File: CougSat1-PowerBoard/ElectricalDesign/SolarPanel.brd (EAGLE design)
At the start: 79 x 90 mm, 120 parts, among them J101 Wire Harness Connector, U1 INA199C2, U100 SPV1040, U101 SPV1040, U2 INA199C2, U3 INA199C2, U4 INA199C2, U5 AD7291, U6 AD7291, U7 AD8515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

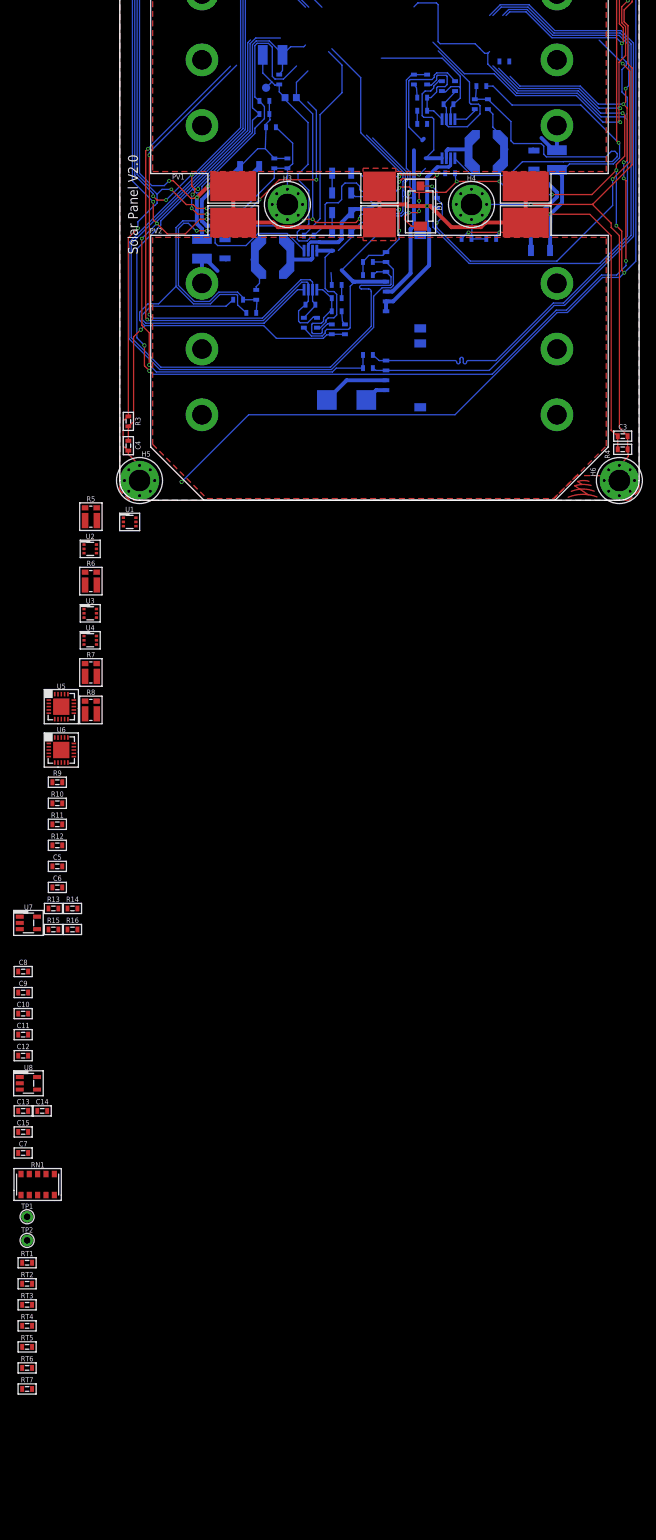
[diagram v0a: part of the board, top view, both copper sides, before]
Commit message: Stuffed addresses on variants, exported PDFs
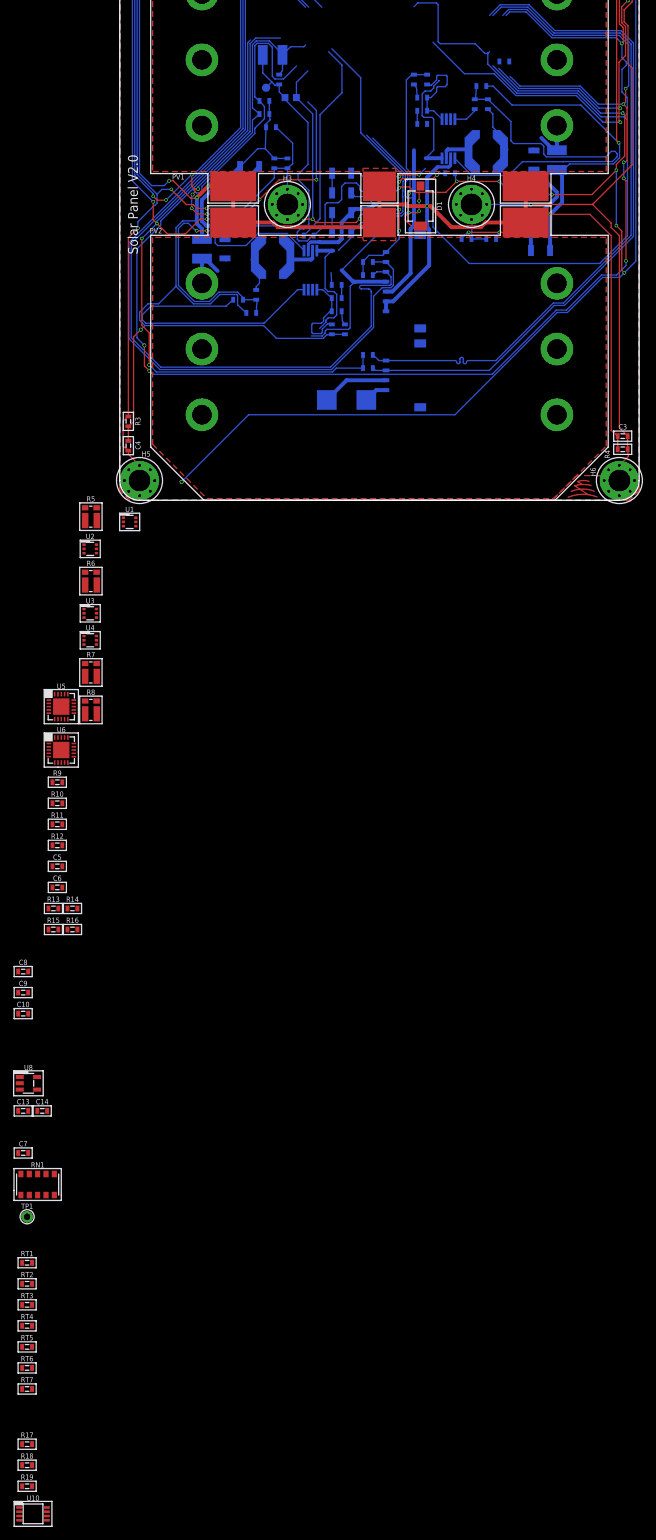
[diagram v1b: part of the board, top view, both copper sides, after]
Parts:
- removed C102, C115, C12: 1µF 10%, CougsInSpace-Capacitors:1608
- removed C11: 10µF 10%, CougsInSpace-Capacitors:1608
- removed C15: 100nF 10%, CougsInSpace-Capacitors:1608
- removed R103, R104, R127, R128: 1kΩ 0.1%, CougsInSpace-Resistors:1608
- removed R115: 150Ω 1%, CougsInSpace-Resistors:1608
- removed TP2: TEST_POINT-THT-1.0, CougsInSpace-Connectors:THT-1.0
- removed U7: AD8515, CougsInSpace-IC-Amplifiers:SOT23-5
- added R17: 10Ω 5%, CougsInSpace-Resistors:1608
- added R18: 33kΩ 1%, CougsInSpace-Resistors:1608
- added R19: 1kΩ 0.1%, CougsInSpace-Resistors:1608
- added U10: AD8542, CougsInSpace-IC-Amplifiers:MSOP-8
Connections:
- net AVREF-1 renamed AVREF
- net N$1 renamed PV_I_N-B
- net N$3 renamed VOUT_N-B
- net N$4 renamed VOUT_P-B
- net N$5 renamed PV_I_N-A
- net N$6 renamed PV_I_P-A
- net N$7 renamed VOUT_N-A
- net N$8 renamed VOUT_P-A
- removed net AVREF-0: C12.1, TP2.1, U7.1, U7.4
- removed net MPPT_ICTRL_N-A: C102.2, R104.1, U100.6
- removed net MPPT_ICTRL_N-B: C115.2, R127.1, U101.6
- removed net MPPT_ICTRL_P-A: C102.1, R103.1, U100.7
- removed net MPPT_ICTRL_P-B: C115.1, R128.1, U101.7
- removed net N$13: C11.1, U5.7, U7.3
- removed net N$16: R5.2-KELVIN
- new net N$1: U101.6, U101.7
- new net PD_AMP_FB: R18.1, R19.2, U10.6
- new net PD_IN: D1.C, R17.1, U10.2
- new net PD_TRANS_OUT: R17.2, U10.1, U10.5
- new net PV_I_P-B: R5.2-KELVIN, U1.4
- net AGND: now also D1.A, R19.1, U10.3, U10.4; no longer C11.2, C12.2, C15.2, R115.1, U7.2
- net AVDD: now also U10.8; no longer C15.1, D1.C, U7.5
- net MPPT_VOUT-A: no longer R103.2
- net MPPT_VOUT-B: no longer R128.2
- net N$2: now also U100.6, U100.7; no longer U1.4
- net PHOTODIODE: now also R18.2, U10.7; no longer D1.A, R115.2
- net VOUT-A: no longer R104.2
- net VOUT-B: no longer R127.2
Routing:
- net MPPT_ICTRL_P-A: track 80.7 -> 0.00 mm, vias 2 -> 0
- net MPPT_ICTRL_N-A: track 77.5 -> 0.00 mm, vias 2 -> 0
- net PHOTODIODE: track 69.6 -> 0.00 mm, vias 4 -> 0
- net MPPT_ICTRL_N-B: track 24.9 -> 0.00 mm
- net MPPT_ICTRL_P-B: track 23.5 -> 0.00 mm
- net VOUT-B: track 55.4 -> 36.9 mm
- net VOUT-A: track 53.4 -> 51.7 mm
- net AVDD: track 292.4 -> 291.0 mm
- net AGND: track 388.7 -> 387.8 mm

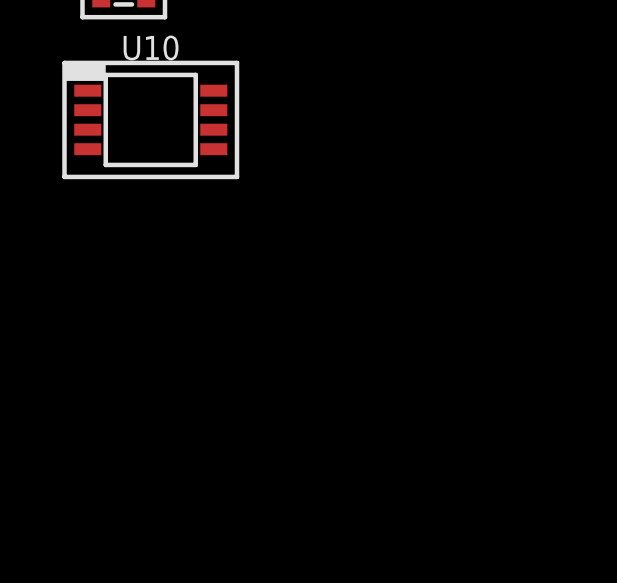
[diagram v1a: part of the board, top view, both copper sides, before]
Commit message: Fixed chematic off-sheet connectors
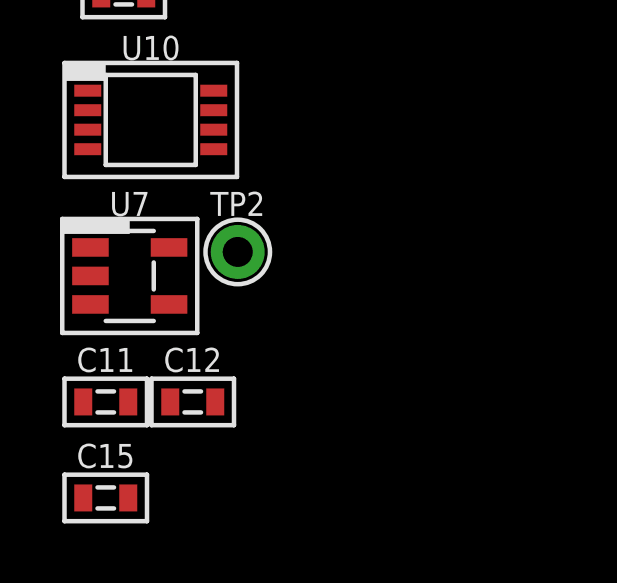
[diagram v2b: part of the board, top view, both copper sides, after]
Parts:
- added C11: 10µF 10%, CougsInSpace-Capacitors:1608
- added C12: 1µF 10%, CougsInSpace-Capacitors:1608
- added C15: 100nF 10%, CougsInSpace-Capacitors:1608
- added TP2: TEST_POINT-THT-1.0, CougsInSpace-Connectors:THT-1.0
- added U7: AD8515, CougsInSpace-IC-Amplifiers:SOT23-5
- J100: value (none) -> ADCS
- J101: value Wire Harness Connector -> EPS
- R100, R101, R110, R112: value 0Ω <20mΩ -> 2.2kΩ 1%
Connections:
- net AVREF renamed AVREF-1
- net N$10 renamed ADC_AS1-EPS
- net N$11 renamed ADC_DCAP-ADCS
- net N$12 renamed ADC_DCAP-EPS
- net N$14 renamed ADC_AS0-ADCS
- net N$15 renamed ADC_AS1-ADCS
- net N$17 renamed ADC_VREF-ADCS
- net N$9 renamed ADC_AS0-EPS
- new net ADC_VREF-EPS: C11.1, U5.7, U7.3
- new net AVREF-0: C12.1, TP2.1, U7.1, U7.4
- net AGND: now also C11.2, C12.2, C15.2, U7.2
- net AVDD: now also C15.1, U7.5
- net VOUT-A: no longer U5.5
- net VOUT-B: no longer U5.4

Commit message: Addressed most feedback points
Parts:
- removed RT100, RT102: 68kΩ 5%, CougsInSpace-Resistors:1608
- added R20, R21: 1kΩ 0.1%, CougsInSpace-Resistors:1608
- added R22, R23: 10kΩ 0.1%, CougsInSpace-Resistors:1608
- added RN2, RN3: 50kΩ 0.1%, CougsInSpace-Resistors:1616
- added RT8, RT9: 10kΩ 5%, CougsInSpace-Resistors:1608
- added TP3, TP4: TEST_POINT-THT-1.0, CougsInSpace-Connectors:THT-1.0
- moved R121 238.0 mm to (-54.1, -221.4), flipped to the top, turned to 0 degrees
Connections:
- net I_PV-A renamed PV_I-A
- net I_PV-B renamed PV_I-B
- removed net N$1: U101.6, U101.7
- removed net N$2: U100.6, U100.7
- removed net PV_IIN_P-A: C105.A, PV2.VCC@1, PV2.VCC@2, PV2.VCC@3, PV2.VCC@4, PV2.VCC@5, PV2.VCC@6, R7.2
- removed net PV_IIN_P-B: C113.A, PV1.VCC@1, PV1.VCC@2, PV1.VCC@3, PV1.VCC@4, PV1.VCC@5, PV1.VCC@6, R5.2
- new net MPPT_ICTRL-A: R20.1, U100.6, U100.7
- new net MPPT_ICTRL-B: R21.1, U101.6, U101.7
- new net PV_V-A: C105.A, PV2.VCC@1, PV2.VCC@2, PV2.VCC@3, PV2.VCC@4, PV2.VCC@5, PV2.VCC@6, R7.2, RN2.2
- new net PV_V-B: C113.A, PV1.VCC@1, PV1.VCC@2, PV1.VCC@3, PV1.VCC@4, PV1.VCC@5, PV1.VCC@6, R5.2, RN3.2
- new net PV_V_SENSE-A: RN2.3, RN2.4, U5.4
- new net PV_V_SENSE-B: RN3.3, RN3.4, U5.5
- net ADC_VREF-ADCS: now also TP4.1
- net ADC_VREF-EPS: now also TP3.1
- net AGND: now also RN2.1, RN3.1, RT8.2, RT9.2
- net AVDD: no longer RT100.1, RT102.1
- net AVREF-0: now also R22.2, R23.2
- net DGND: now also R121.2
- net MPPT_VOUT-A: now also R20.2
- net MPPT_VOUT-B: now also R21.2
- net PGND: no longer R121.2
- net TEMP_MPPT-A: now also R22.1, RT9.1; no longer RT100.2
- net TEMP_MPPT-B: now also R23.1, RT8.1; no longer RT102.2
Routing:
- net AGND: track 387.8 -> 22.7 mm, vias 11 -> 0
- net AVDD: track 291.0 -> 37.7 mm, vias 13 -> 0
- net TEMP_MPPT-B: track 32.5 -> 0.00 mm, vias 2 -> 0
- net TEMP_MPPT-A: track 31.2 -> 0.00 mm
- net PV_V-B: track 0.00 -> 6.89 mm
- net PV_V-A: track 0.00 -> 6.89 mm
- net PV_IIN_P-B: track 6.89 -> 0.00 mm
- net PV_IIN_P-A: track 6.89 -> 0.00 mm
- net PGND: track 439.5 -> 436.7 mm
- added copper zone on layer 1, net PV_V-A
- added copper zone on layer 1, net PV_V-B
- removed copper zone on layer 1, net PV_IIN_P-A
- removed copper zone on layer 1, net PV_IIN_P-B

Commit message: Updated photodiode circuit
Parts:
- removed L101, L102: 10µH 20%, CougsInSpace-Coils:6060
- removed R18: 33kΩ 1%, CougsInSpace-Resistors:1608
- removed R19: 1kΩ 0.1%, CougsInSpace-Resistors:1608
- removed U10: AD8542, CougsInSpace-IC-Amplifiers:MSOP-8
- added L1, L2: 10µH 30%, CougsInSpace-Coils:SRU1038
- R17: value 10Ω 5% -> 2kΩ 0.1%
- moved R17 64.4 mm to (-53.6, -253.0)
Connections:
- removed net PD_AMP_FB: R18.1, R19.2, U10.6
- removed net PD_IN: D1.C, R17.1, U10.2
- removed net PD_TRANS_OUT: R17.2, U10.1, U10.5
- net 3.3V: now also D1.C
- net AGND: now also R17.1; no longer D1.A, R19.1, U10.3, U10.4
- net AVDD: no longer U10.8
- net CHASSIS: now also H1.V10, H1.V9, H2.V10, H2.V9, H3.V10, H3.V9, H4.V10, H4.V9, H5.V10, H5.V9, H6.V10, H6.V9
- net MPPT_LX-A: now also L2.2; no longer L101.2
- net MPPT_LX-B: now also L1.2; no longer L102.2
- net PHOTODIODE: now also D1.A, R17.2; no longer R18.2, U10.7
- net PV_IIN_N-A: now also L2.1; no longer L101.1
- net PV_IIN_N-B: now also L1.1; no longer L102.1
- net PV_V-A: no longer PV2.VCC@5, PV2.VCC@6
- net PV_V-B: no longer PV1.VCC@5, PV1.VCC@6
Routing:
- net CHASSIS: track 408.4 -> 414.1 mm
- net PV_IIN_N-B: track 8.29 -> 5.69 mm
- net MPPT_LX-B: track 4.75 -> 4.21 mm
- net MPPT_LX-A: track 4.76 -> 4.22 mm

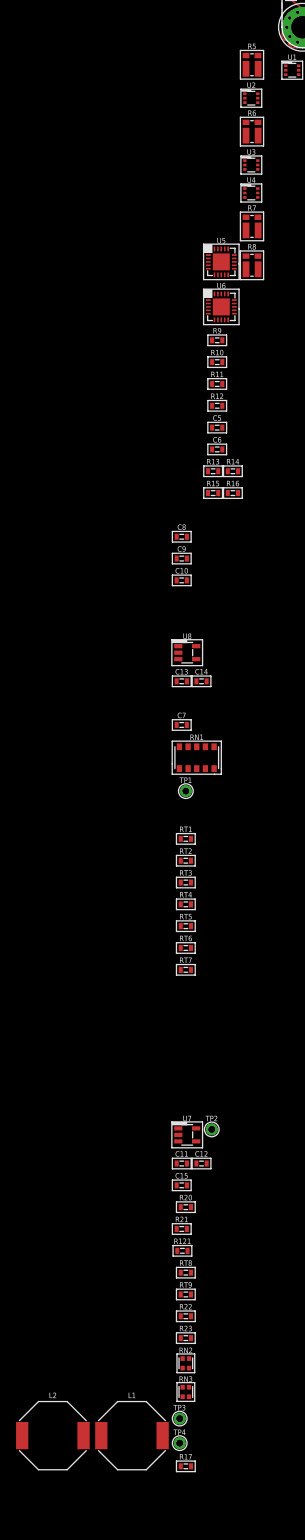
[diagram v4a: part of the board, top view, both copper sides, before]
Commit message: Addressed feedback, exported PDFs
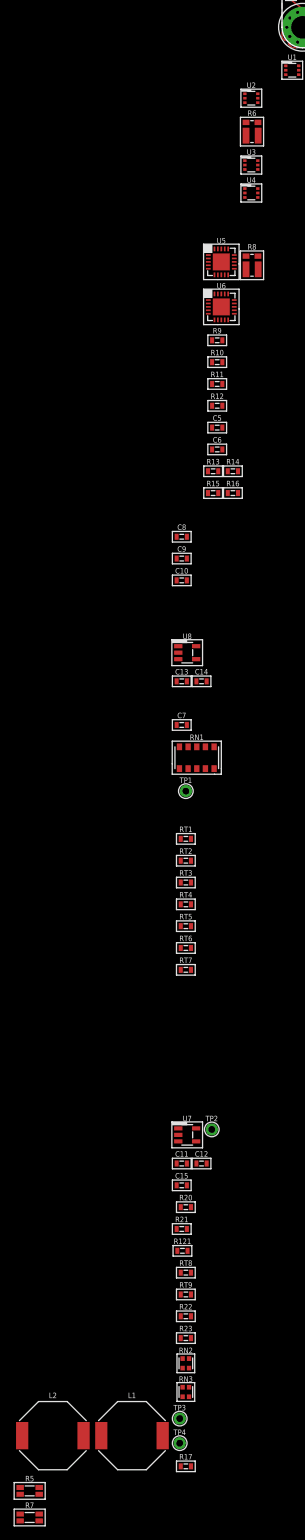
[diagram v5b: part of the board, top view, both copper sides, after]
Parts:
- R5, R7: value 5mΩ 1% -> 12mΩ 1%; device CougsInSpace-Resistors:1632-KELVIN -> CougsInSpace-Resistors:3216-KELVIN
- moved R5 211.6 mm to (-76.5, -256.6)
- moved R7 192.1 mm to (-76.5, -260.5)

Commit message: Fixed photodiode circuit
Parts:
- R17: value 2kΩ 0.1% -> 1.33kΩ 0.1%
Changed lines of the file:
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@@
 <?xml version="1.0" encoding="utf-8"?>
 <!DOCTYPE eagle SYSTEM "eagle.dtd">
-<eagle version="9.5.1">
+<eagle version="9.5.2">
 <drawing>
 <settings>
@@
 <attribute name="NAME" x="-54.5" y="-248" size="0.8" layer="25" font="vector" ratio="15" align="center"/>
 </element>
-<element name="R17" library="CougsInSpace-Resistors" package="1608" value="2kΩ 0.1%" x="-53.6" y="-253" smashed="yes">
+<element name="R17" library="CougsInSpace-Resistors" package="1608" value="1.33kΩ 0.1%" x="-53.6" y="-253" smashed="yes">
 <attribute name="NAME" x="-53.6" y="-251.6" size="0.8" layer="25" font="vector" ratio="15" align="center"/>
 <attribute name="PACKAGE" value="1608" x="-53.6" y="-253" size="1.778" layer="27" display="off"/>
-<attribute name="POWER" value="1/10W" x="-53.6" y="-253" size="1.778" layer="27" display="off"/>
-<attribute name="SKU" value="21-2001" x="-53.6" y="-253" size="1.778" layer="27" display="off"/>
-<attribute name="TEMP" value="25ppm/°C" x="-53.6" y="-253" size="1.778" layer="27" display="off"/>
+<attribute name="POWER" value="1/5W" x="-53.6" y="-253" size="1.778" layer="27" display="off"/>
+<attribute name="SKU" value="21-1331" x="-53.6" y="-253" size="1.778" layer="27" display="off"/>
+<attribute name="TEMP" value="50ppm/°C" x="-53.6" y="-253" size="1.778" layer="27" display="off"/>
 </element>
 <element name="L1" library="CougsInSpace-Coils" package="SRU1038" value="10µH 30%" x="-61.5" y="-248.5" smashed="yes">

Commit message: Addressed all feedback
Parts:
- removed C12, C14: 1µF 10%, CougsInSpace-Capacitors:1608
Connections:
- net AGND: no longer C12.2, C14.2
- net AVREF-0: no longer C12.1
- net AVREF-1: no longer C14.1

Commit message: Placed most components for battery chargers
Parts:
- L1, L2: value 10µH 30% -> 10µH 20%; device CougsInSpace-Coils:SRU1038 -> CougsInSpace-Coils:6060
- R17: value 1.33kΩ 0.1% -> 1.2kΩ 0.1%
- moved R5 282.3 mm to (17.8, 9.50), flipped to the bottom, turned to 180 degrees
- moved L1 267.0 mm to (9.00, 9.00), flipped to the bottom
- moved R7 257.8 mm to (-17.8, -9.50), flipped to the bottom
- moved L2 247.9 mm to (-9.00, -9.00), flipped to the bottom, turned to 180 degrees
- moved R21 232.4 mm to (-4.25, 8.75), flipped to the bottom, turned to 90 degrees
- moved R20 214.2 mm to (4.25, -8.75), flipped to the bottom, turned to 270 degrees
- moved U6 146.1 mm to (56.5, 18.8), flipped to the bottom
- moved R8 81.0 mm to (5.25, -12.5), flipped to the bottom, turned to 180 degrees
- moved R6 79.8 mm to (-5.25, 12.5), flipped to the bottom
- moved U2 77.9 mm to (-14.0, 19.5), flipped to the bottom
- moved LOGO100 71.5 mm to (87.1, -24.9)
- moved L100 38.2 mm to (25.5, -52.8)
- moved R119 37.6 mm to (-52.2, 23.2)
- moved C119 37.6 mm to (56.5, 23.8)
- moved FB100 34.1 mm to (-46.2, 25.8)
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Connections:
- net MPPT_VOUT-A: now also R8.1; no longer R8.2
- net MPPT_VOUT-B: now also R6.1; no longer R6.2
- net VOUT-A: now also R8.2; no longer R8.1
- net VOUT-B: now also R6.2; no longer R6.1
- net VOUT_N-A: now also R8.2-KELVIN; no longer R8.1-KELVIN
- net VOUT_N-B: now also R6.2-KELVIN; no longer R6.1-KELVIN
- net VOUT_P-A: now also R8.1-KELVIN; no longer R8.2-KELVIN
- net VOUT_P-B: now also R6.1-KELVIN; no longer R6.2-KELVIN
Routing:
- net PGND: track 436.7 -> 0.00 mm, vias 12 -> 0
- net CHASSIS: track 414.1 -> 0.00 mm, vias 5 -> 0
- net 3.3V: track 370.0 -> 0.00 mm, vias 13 -> 0
- net DGND: track 258.2 -> 0.00 mm, vias 7 -> 0
- net I2C_SDA_PMIC: track 126.4 -> 0.00 mm
- net I2C_SCL_PMIC: track 126.1 -> 0.00 mm
- net I2C_SCL_ADCS: track 102.6 -> 0.00 mm
- net I2C_SDA_ADCS: track 101.7 -> 0.00 mm
- net MPPT_SET-B: track 57.7 -> 0.00 mm
- net VOUT-A: track 51.7 -> 0.00 mm
- net MPPT_SET-A: track 48.4 -> 0.00 mm, vias 2 -> 0
- net X_SHUT-A: track 42.5 -> 0.00 mm
- net AVDD: track 37.8 -> 0.00 mm
- net VOUT-B: track 36.9 -> 0.00 mm
- net MPPT_VOUT-B: track 30.7 -> 0.00 mm, vias 2 -> 0
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- removed copper zone on layer 16, net BALANCING
- removed copper zone on layer 1, net BALANCING1
- removed copper zone on layer 1, net PV_V-A
- removed copper zone on layer 1, net PV_V-B
